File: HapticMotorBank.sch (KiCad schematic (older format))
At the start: 0 parts

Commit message: Added components
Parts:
- added U?: 74LS251, symbol 74LS251
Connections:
- net labels added: GND
- wire segments 0 -> 4
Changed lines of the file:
@@
 Comment4 ""
 $EndDescr
+$Comp
+L 74LS251 U?
+U 1 1 58CAE2D5
+P 6750 2850
+F 0 "U?" H 6750 2850 50  0000 C CNN
+F 1 "74LS251" H 6750 2700 50  0000 C CNN
+F 2 "" H 6750 2850 50  0000 C CNN
+F 3 "" H 6750 2850 50  0000 C CNN
+	1    6750 2850
+	1    0    0    -1
+$EndComp
+Wire Wire Line
+	3700 2200 6050 2200
+Wire Wire Line
+	3700 2200 3700 1900
+Wire Wire Line
+	6050 3500 5800 3500
+Wire Wire Line
+	5800 3500 5800 4150
+$Comp
+L GND #PWR?
+U 1 1 58CAE30D
+P 5800 4150
+F 0 "#PWR?" H 5800 3900 50  0001 C CNN
+F 1 "GND" H 5800 4000 50  0000 C CNN
+F 2 "" H 5800 4150 50  0000 C CNN
+F 3 "" H 5800 4150 50  0000 C CNN
+	1    5800 4150
+	1    0    0    -1
+$EndComp
 $EndSCHEMATC

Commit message: Rev 1 Schematics
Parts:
- removed U?: 74LS251, symbol 74LS251
- added P? (x2): CONN_01X04, symbol CONN_01X04
- added P?: Trigger1, symbol CONN_01X01
- added P?: Trigger2, symbol CONN_01X01
- added P?: Trigger3, symbol CONN_01X01
- added P?: Trigger4, symbol CONN_01X01
- added P?: Trigger5, symbol CONN_01X01
- added P?: Trigger6, symbol CONN_01X01
- added R? (x2): 33, symbol R_Small
- added U?: CD4051B, SMD_Packages:SO-16-N, symbol CD4051B
- added U? (x3): 74LVC1T45, TO_SOT_Packages_SMD:SOT-363_SC-70-6_Handsoldering, symbol 74LVC1T45
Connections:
- net labels added: +1V2, 5V, PinTrigger1, PinTrigger2, PinTrigger3, SCL, SDA
- wire segments 4 -> 60
- no-connect marks 0 -> 3
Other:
- note added: "Bus end"
- note added: "Bus start"
- note added: "Haptic Motor Bank"
- note added: "Level Shifters -> Reverse Direction"
- note added: "Output Triggers"

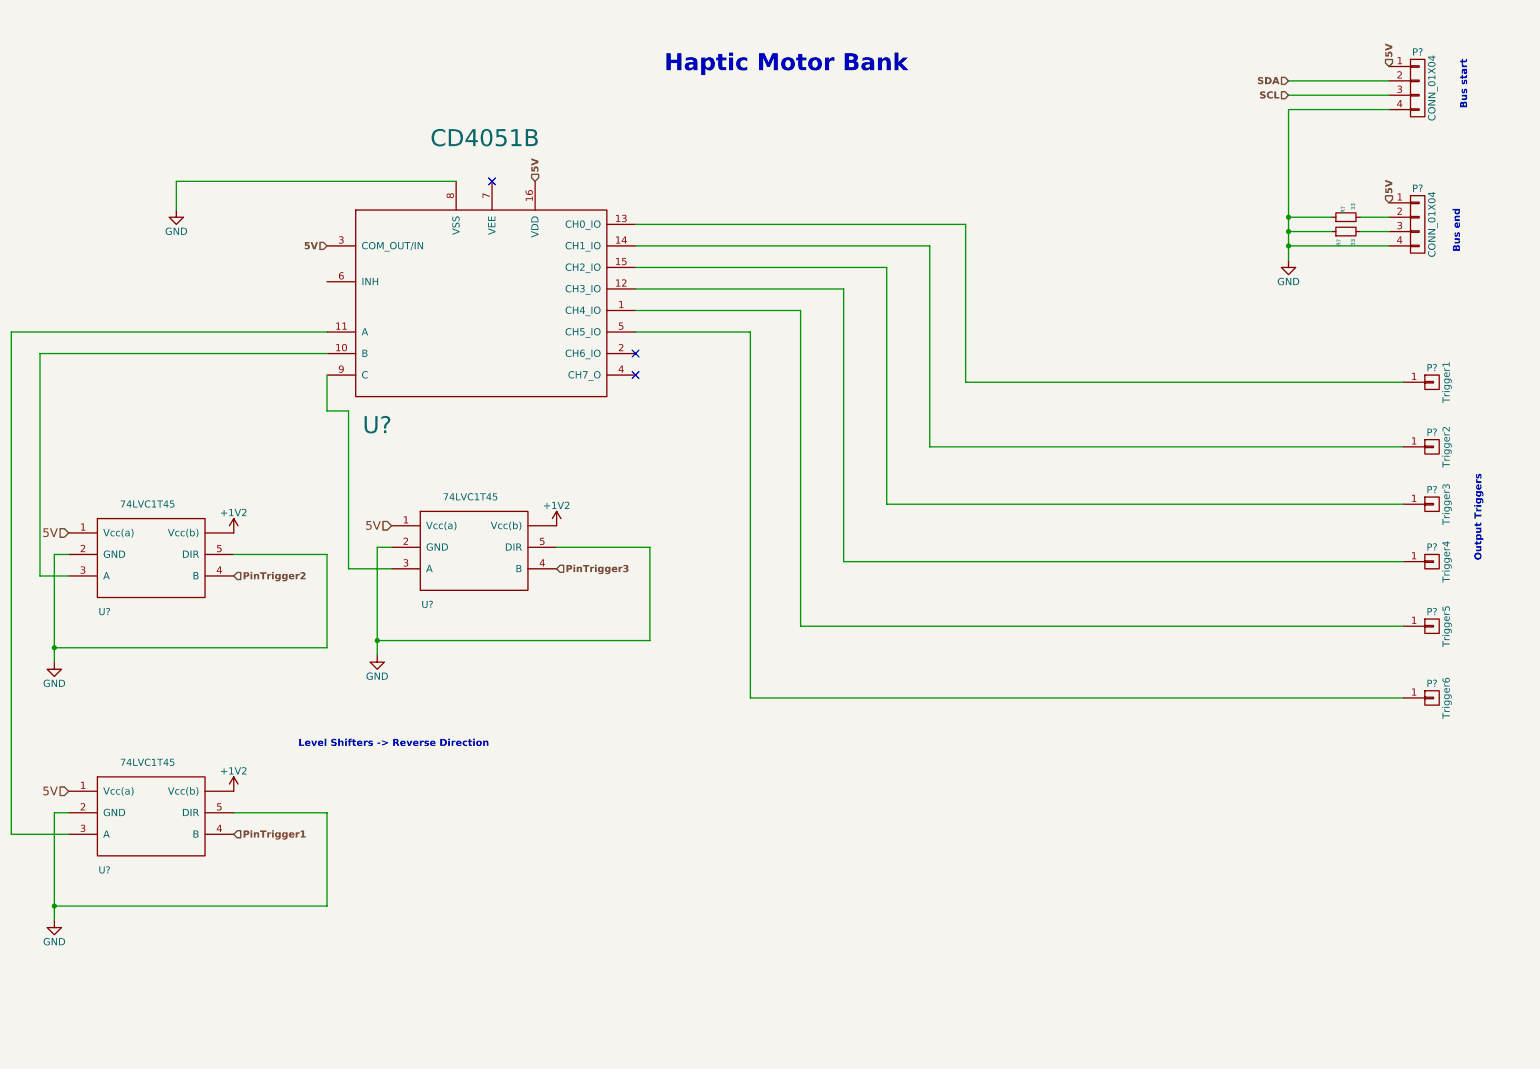
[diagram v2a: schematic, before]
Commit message: added DRV breakout board to haptic motor bank schematic
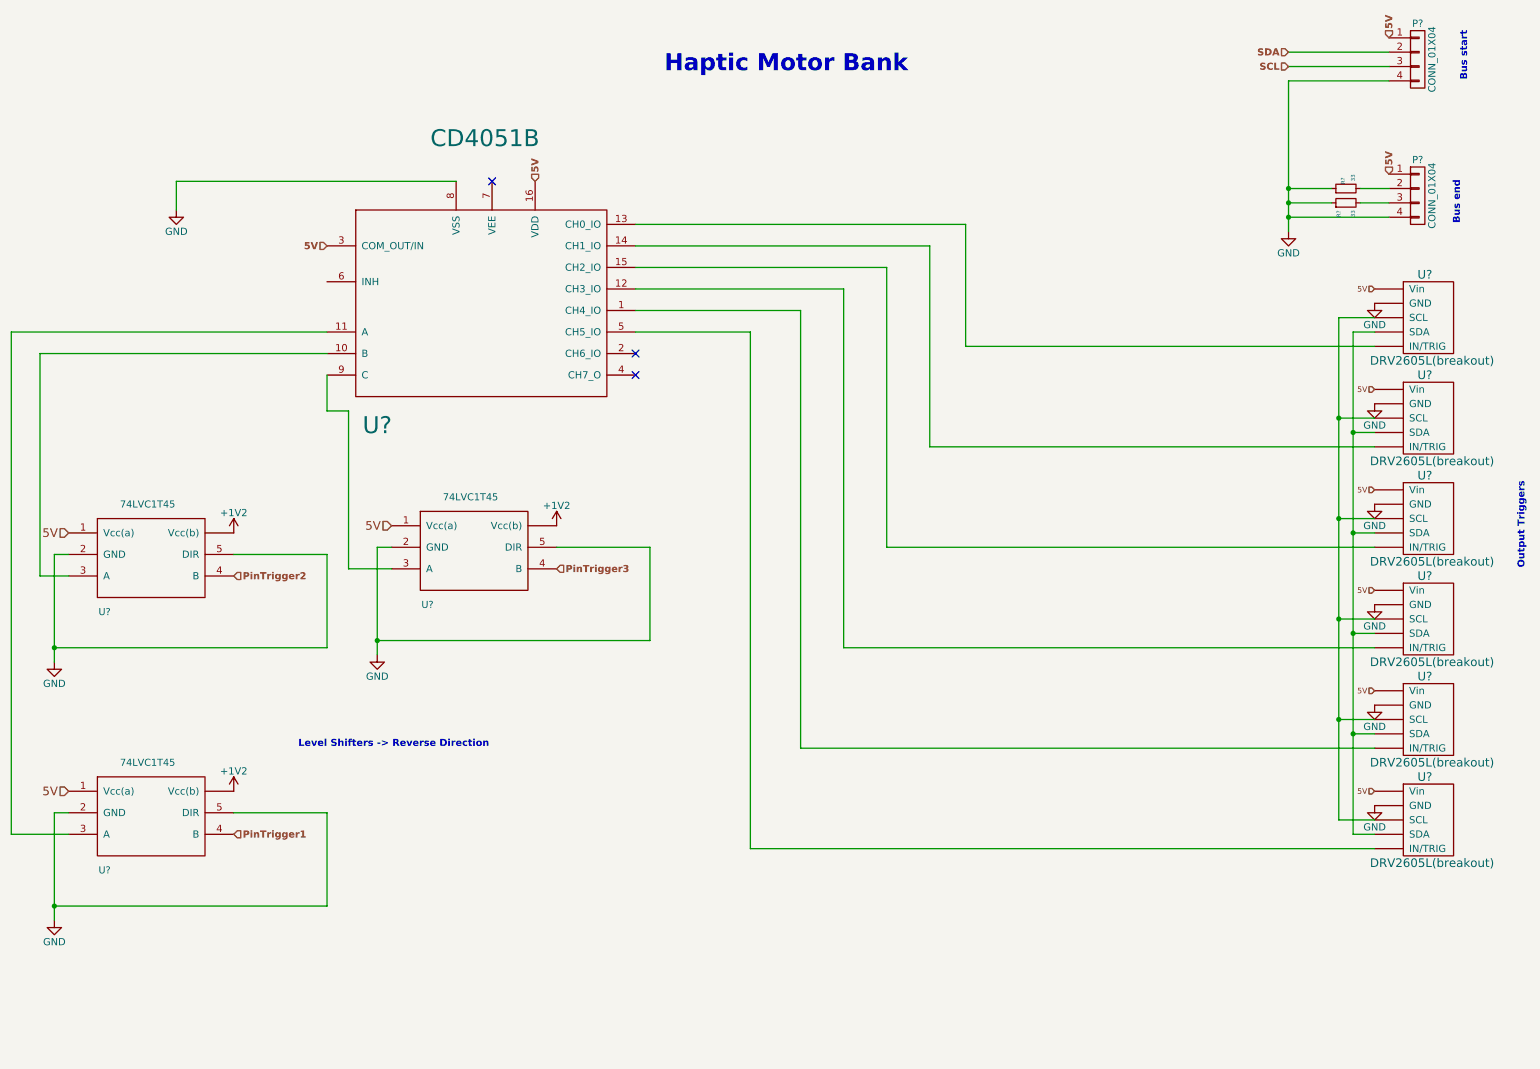
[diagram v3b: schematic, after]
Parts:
- removed P?: Trigger1, symbol CONN_01X01
- removed P?: Trigger2, symbol CONN_01X01
- removed P?: Trigger3, symbol CONN_01X01
- removed P?: Trigger4, symbol CONN_01X01
- removed P?: Trigger5, symbol CONN_01X01
- removed P?: Trigger6, symbol CONN_01X01
- added U? (x6): DRV2605L(breakout), symbol DRV2605L(breakout)
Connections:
- net 5V: now also U?.~ (Vin), U?.~ (Vin), U?.~ (Vin), U?.~ (Vin), U?.~ (Vin), U?.~ (Vin)
- net GND: now also U?.~ (Vin), U?.~ (Vin), U?.~ (Vin), U?.~ (Vin), U?.~ (Vin), U?.~ (Vin)
- net at U?.1 (CH4_IO): now also U?.~ (Vin)
- net at U?.12 (CH3_IO): now also U?.~ (Vin)
- net at U?.13 (CH0_IO): now also U?.~ (Vin)
- net at U?.14 (CH1_IO): now also U?.~ (Vin)
- net at U?.15 (CH2_IO): now also U?.~ (Vin)
- net at U?.5 (CH5_IO): now also U?.~ (Vin)
- new net: U?.~ (Vin), U?.~ (Vin), U?.~ (Vin), U?.~ (Vin), U?.~ (Vin), U?.~ (Vin) (x2)
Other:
- moved on the sheet: P?, R?

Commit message: More GPIO Pins Available
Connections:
- new net: U?.~ (Vin), U?.~ (Vin), U?.~ (Vin), U?.~ (Vin), U?.~ (Vin), U?.~ (Vin) (x2)
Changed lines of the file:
@@
 LIBS:valves
 LIBS:iSight360
+LIBS:AVE-NvidiaTX1-ISight360-cache
 EELAYER 25 0
 EELAYER END
 $Descr A4 11693 8268
 encoding utf-8
-Sheet 1 1
+Sheet 4 5
 Title "Haptic Motor Bank"
 Date "2017-03-17"

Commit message: Rev .99999 w/ Layout
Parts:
- added JP401: CTRL Jump1, Pin_Headers:Pin_Header_Straight_1x03_Pitch2.54mm_SMD_Pin1Left, symbol Jumper_NC_Dual
- added JP402: CTRL Jump2, Pin_Headers:Pin_Header_Straight_1x03_Pitch2.54mm_SMD_Pin1Left, symbol Jumper_NC_Dual
- added JP403: CTRL Jump3, Pin_Headers:Pin_Header_Straight_1x03_Pitch2.54mm_SMD_Pin1Left, symbol Jumper_NC_Dual
- P401, P402: renamed from P?; footprint (none) -> Pin_Headers:Pin_Header_Angled_1x04_Pitch2.54mm
- R401, R402: renamed from R?; footprint (none) -> Resistors_SMD:R_1206_HandSoldering
- U405, U406, U407, U408, U409, U410: renamed from U?; footprint (none) -> Pin_Headers:Pin_Header_Angled_1x04_Pitch2.54mm
- gave numbers to parts that had none: 4
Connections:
- net PinTrigger1: now also JP401.1
- net PinTrigger2: now also JP402.1
- net PinTrigger3: now also JP403.1
- net at U404.10 (B): now also JP402.2; no longer U401.3 (A)
- net at U404.11 (A): now also JP401.2; no longer U402.3 (A)
- net at U404.9 (C): now also JP403.2; no longer U403.3 (A)
- new net: JP402.3, U401.3 (A)
- new net: JP403.3, U403.3 (A)
- new net: JP401.3, U402.3 (A)
- new net: U405.~ (Vin), U406.~ (Vin), U407.~ (Vin), U408.~ (Vin), U409.~ (Vin), U410.~ (Vin) (x2)
- no-connect marks 3 -> 4
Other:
- note added: "Selectable Inputs"
- moved on the sheet: U401, U402, U403
